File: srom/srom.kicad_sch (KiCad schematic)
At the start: 20 parts, among them J1 Conn_01x03_Female, Q1 PMBT2222A, U1 4075, U4 74LS245, U5 Pico-1 ROM

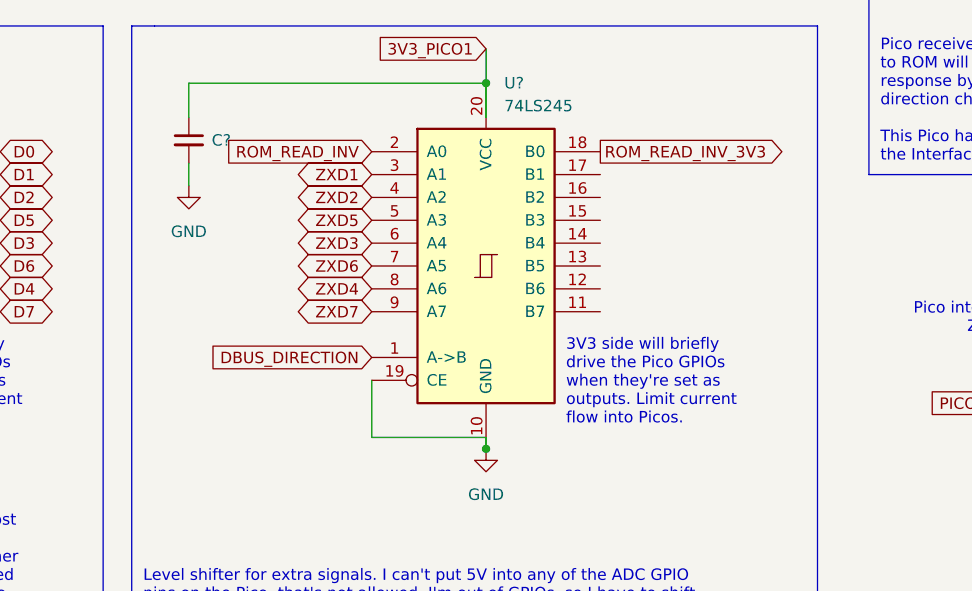
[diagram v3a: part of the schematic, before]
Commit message: update schematic to match current hardware
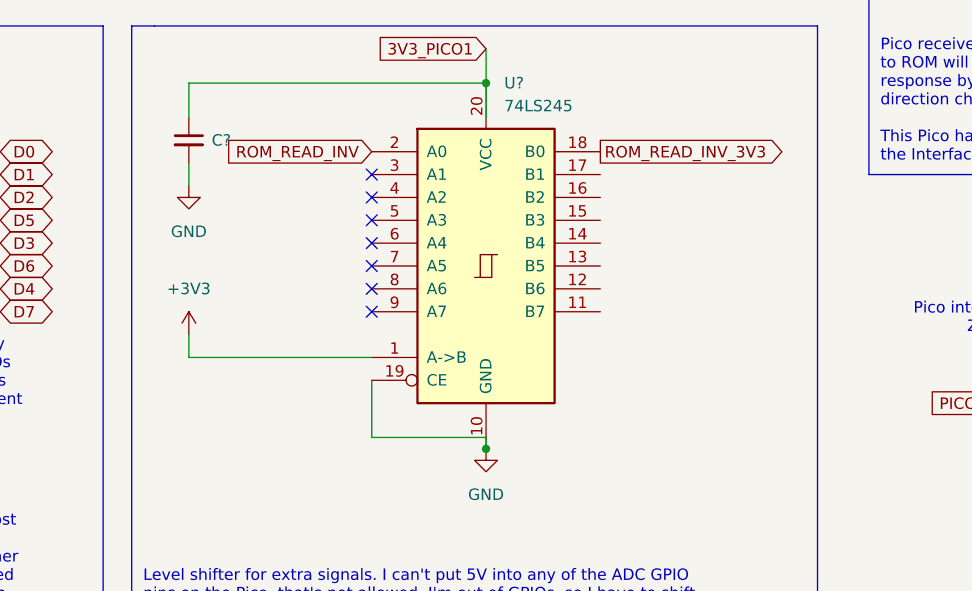
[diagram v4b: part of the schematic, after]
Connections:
- net DBUS_DIRECTION: no longer U?.1 (A->B)
- net ZXD1: no longer U?.3 (A1)
- net ZXD2: no longer U?.4 (A2)
- net ZXD3: no longer U?.6 (A4)
- net ZXD4: no longer U?.8 (A6)
- net ZXD5: no longer U?.5 (A3)
- net ZXD6: no longer U?.7 (A5)
- net ZXD7: no longer U?.9 (A7)
- new net +3V3: U?.1 (A->B)
- no-connect marks 27 -> 34
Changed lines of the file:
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@@
   (junction (at 132.715 156.21) (diameter 0) (color 0 0 0 0)
   )
+  (no_connect (at 120.015 125.73))
   (no_connect (at 54.61 62.23))
   (no_connect (at 54.61 29.21))
+  (no_connect (at 120.015 140.97))
   (no_connect (at 142.24 44.45))
   (no_connect (at 54.61 67.31))
+  (no_connect (at 120.015 128.27))
   (no_connect (at 26.67 29.21))
+  (no_connect (at 120.015 135.89))
   (no_connect (at 54.61 85.09))
+  (no_connect (at 120.015 133.35))
   (no_connect (at 26.67 57.15))
   (no_connect (at 54.61 59.69))
   (no_connect (at 54.61 57.15))
+  (no_connect (at 120.015 130.81))
   (no_connect (at 242.57 36.83))
   (no_connect (at 142.24 46.99))
@@
   (no_connect (at 26.67 52.07))
   (no_connect (at 142.24 41.91))
+  (no_connect (at 120.015 138.43))
   (no_connect (at 54.61 64.77))
   (no_connect (at 157.48 44.45))
@@
     (stroke (width 0) (type default) (color 0 0 0 0))
   )
+  (wire (pts (xy 99.695 143.51) (xy 99.695 146.05))
+    (stroke (width 0) (type default) (color 0 0 0 0))
+  )
   (polyline (pts (xy 280.67 125.73) (xy 175.26 125.73))
     (stroke (width 0) (type default) (color 0 0 0 0))
@@
   )
   (polyline (pts (xy 179.07 15.24) (xy 280.67 15.24))
+    (stroke (width 0) (type default) (color 0 0 0 0))
+  )
+  (wire (pts (xy 120.015 146.05) (xy 99.695 146.05))
     (stroke (width 0) (type default) (color 0 0 0 0))
   )
@@
     (effects (font (size 1.27 1.27)) (justify left bottom))
   )
-  (text "3V3 side will briefly\ndrive the Pico GPIOs\nwhen they're set as\noutputs. Limit current\nflow into Picos."
-    (at 141.605 153.67 0)
-    (effects (font (size 1.27 1.27)) (justify left bottom))
-  )
   (text "Level shifter for the data bus. Permanently enabled (unlike in the ROM\nemulator project). Direction is driven by the DBUS_DIRECTION signal. Most\ntimes that's high so the direction is ZX->Pico. The Pico therefore gets to\nsee any data the ZX writes pretty much immediately. During a read, either\n/MREQ or /IORQ, the direction is reversed by the signal which is generated\nvia a PIO program running on the IO Pico. That PIO responds to either the\n/MREQ or /IORQ, both of which the IO Pico can see."
     (at 15.24 175.26 0)
@@
     (effects (font (size 1.27 1.27)) (justify left bottom))
   )
-  (global_label "ZXD5" (shape bidirectional) (at 120.015 130.81 180) (fields_autoplaced)
-    (effects (font (size 1.27 1.27)) (justify right))
-    (property "Intersheet References" "${INTERSHEET_REFS}" (id 0) (at 112.7033 130.7306 0)
-      (effects (font (size 1.27 1.27)) (justify right) hide)
-    )
-  )
   (global_label "ZXD1" (shape bidirectional) (at 26.67 36.83 180) (fields_autoplaced)
     (effects (font (size 1.27 1.27)) (justify right))
@@
     )
   )
-  (global_label "DBUS_DIRECTION" (shape input) (at 120.015 146.05 180) (fields_autoplaced)
-    (effects (font (size 1.27 1.27)) (justify right))
-    (property "Intersheet References" "${INTERSHEET_REFS}" (id 0) (at 101.7571 145.9706 0)
-      (effects (font (size 1.27 1.27)) (justify right) hide)
-    )
-  )
   (global_label "D4" (shape input) (at 207.01 49.53 180) (fields_autoplaced)
     (effects (font (size 1.27 1.27)) (justify right))
@@
     )
   )
-  (global_label "ZXD7" (shape bidirectional) (at 120.015 140.97 180) (fields_autoplaced)
-    (effects (font (size 1.27 1.27)) (justify right))
-    (property "Intersheet References" "${INTERSHEET_REFS}" (id 0) (at 112.7033 140.8906 0)
-      (effects (font (size 1.27 1.27)) (justify right) hide)
-    )
-  )
   (global_label "ZXA1" (shape output) (at 54.61 44.45 0) (fields_autoplaced)
     (effects (font (size 1.27 1.27)) (justify left))
@@
     )
   )
-  (global_label "ZXD4" (shape bidirectional) (at 120.015 138.43 180) (fields_autoplaced)
-    (effects (font (size 1.27 1.27)) (justify right))
-    (property "Intersheet References" "${INTERSHEET_REFS}" (id 0) (at 112.7033 138.3506 0)
-      (effects (font (size 1.27 1.27)) (justify right) hide)
-    )
-  )
-  (global_label "ZXD3" (shape bidirectional) (at 120.015 133.35 180) (fields_autoplaced)
-    (effects (font (size 1.27 1.27)) (justify right))
-    (property "Intersheet References" "${INTERSHEET_REFS}" (id 0) (at 112.7033 133.2706 0)
-      (effects (font (size 1.27 1.27)) (justify right) hide)
-    )
-  )
   (global_label "ZXA14" (shape input) (at 87.63 44.45 180) (fields_autoplaced)
     (effects (font (size 1.27 1.27)) (justify right))
@@
     )
   )
-  (global_label "ZXD1" (shape bidirectional) (at 120.015 125.73 180) (fields_autoplaced)
-    (effects (font (size 1.27 1.27)) (justify right))
-    (property "Intersheet References" "${INTERSHEET_REFS}" (id 0) (at 112.7033 125.6506 0)
-      (effects (font (size 1.27 1.27)) (justify right) hide)
-    )
-  )
   (global_label "ZXA6" (shape input) (at 242.57 57.15 0) (fields_autoplaced)
     (effects (font (size 1.27 1.27)) (justify left))
@@
     )
   )
-  (global_label "ZXD6" (shape bidirectional) (at 120.015 135.89 180) (fields_autoplaced)
-    (effects (font (size 1.27 1.27)) (justify right))
-    (property "Intersheet References" "${INTERSHEET_REFS}" (id 0) (at 112.7033 135.8106 0)
-      (effects (font (size 1.27 1.27)) (justify right) hide)
-    )
-  )
   (global_label "ZXD5" (shape bidirectional) (at 40.64 130.81 180) (fields_autoplaced)
     (effects (font (size 1.27 1.27)) (justify right))
@@
     (effects (font (size 1.27 1.27)) (justify right))
     (property "Intersheet References" "${INTERSHEET_REFS}" (id 0) (at 198.6702 62.1506 0)
-      (effects (font (size 1.27 1.27)) (justify right) hide)
-    )
-  )
-  (global_label "ZXD2" (shape bidirectional) (at 120.015 128.27 180) (fields_autoplaced)
-    (effects (font (size 1.27 1.27)) (justify right))
-    (property "Intersheet References" "${INTERSHEET_REFS}" (id 0) (at 112.7033 128.1906 0)
       (effects (font (size 1.27 1.27)) (justify right) hide)
     )
@@
     )
     (property "Datasheet" "" (id 3) (at 53.34 156.21 0)
+      (effects (font (size 1.27 1.27)) hide)
+    )
+    (pin "1")
+  )
+  (symbol (lib_id "power:+3V3") (at 99.695 143.51 0) (unit 1)
+    (in_bom yes) (on_board yes) (fields_autoplaced)
+    (property "Reference" "#PWR?" (id 0) (at 99.695 147.32 0)
+      (effects (font (size 1.27 1.27)) hide)
+    )
+    (property "Value" "+3V3" (id 1) (at 99.695 138.43 0))
+    (property "Footprint" "" (id 2) (at 99.695 143.51 0)
+      (effects (font (size 1.27 1.27)) hide)
+    )
+    (property "Datasheet" "" (id 3) (at 99.695 143.51 0)
       (effects (font (size 1.27 1.27)) hide)
     )
@@
       (reference "#PWR?") (unit 1) (value "GND") (footprint "")
     )
+    (path "/7a0c9d83-3cea-4fe4-af9e-3086b3ce2ec9"
+      (reference "#PWR?") (unit 1) (value "+3V3") (footprint "")
+    )
     (path "/e8761be2-d56d-4ac2-8a7f-faeaa815f5d5"

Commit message: start updating schematic for next board
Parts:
- gave numbers to parts that had none: 2
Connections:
- net +3V3 is gone; now on net 3V3_PICO1: U101.1 (A->B)
- net D3: now also U5.5 (GPIO3); no longer U5.6 (GPIO4)
- net D4: now also U5.6 (GPIO4); no longer U5.9 (GPIO6)
- net D5: now also U5.7 (GPIO5); no longer U5.5 (GPIO3)
- net D6: now also U5.9 (GPIO6); no longer U5.7 (GPIO5)
- net ROM_READ_INV_3V3: now also U5.31 (GPIO26_ADC0); no longer U5.11 (GPIO8)
- net ZXA0: now also U5.11 (GPIO8); no longer U5.15 (GPIO11)
- net ZXA1: now also U5.12 (GPIO9); no longer U5.16 (GPIO12)
- net ZXA10: now also U5.24 (GPIO18); no longer U5.22 (GPIO17)
- net ZXA11: now also U5.25 (GPIO19); no longer U5.21 (GPIO16)
- net ZXA12: now also U5.26 (GPIO20); no longer U5.14 (GPIO10)
- net ZXA13: now also U5.27 (GPIO21); no longer U5.12 (GPIO9)
- net ZXA2: now also U5.14 (GPIO10); no longer U5.17 (GPIO13)
- net ZXA3: now also U5.15 (GPIO11); no longer U5.19 (GPIO14)
- net ZXA4: now also U5.16 (GPIO12); no longer U5.26 (GPIO20)
- net ZXA5: now also U5.17 (GPIO13); no longer U5.27 (GPIO21)
- net ZXA6: now also U5.19 (GPIO14); no longer U5.29 (GPIO22)
- net ZXA7: now also U5.20 (GPIO15); no longer U5.31 (GPIO26_ADC0)
- net ZXA8: now also U5.21 (GPIO16); no longer U5.25 (GPIO19)
- net ZXA9: now also U5.22 (GPIO17); no longer U5.24 (GPIO18)
- net ZXM1: now also U5.29 (GPIO22); no longer U5.20 (GPIO15)
- net IF1_PORT_ACTIVE: now reaches U5.32 (GPIO27_ADC1)
- no-connect marks 34 -> 40

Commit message: first draft of layout of board 2
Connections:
- net D3: now also R104.2; no longer R105.2
- net D4: now also R105.2; no longer R107.2
- net D5: now also R106.2; no longer R104.2
- net D6: now also R107.2; no longer R106.2
- net ZXD3: now also U4.5 (A3); no longer U4.6 (A4)
- net ZXD4: now also U4.6 (A4); no longer U4.8 (A6)
- net ZXD5: now also U4.7 (A5); no longer U4.5 (A3)
- net ZXD6: now also U4.8 (A6); no longer U4.7 (A5)
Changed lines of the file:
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@@
     )
   )
-  (global_label "D4" (shape bidirectional) (at 78.74 138.43 0) (fields_autoplaced)
+  (global_label "D6" (shape bidirectional) (at 78.74 138.43 0) (fields_autoplaced)
     (effects (font (size 1.27 1.27)) (justify left))
     (property "Intersheet References" "${INTERSHEET_REFS}" (id 0) (at 83.6326 138.3506 0)
@@
     )
   )
-  (global_label "ZXD6" (shape bidirectional) (at 40.64 135.89 180) (fields_autoplaced)
+  (global_label "ZXD5" (shape bidirectional) (at 40.64 135.89 180) (fields_autoplaced)
     (effects (font (size 1.27 1.27)) (justify right))
     (property "Intersheet References" "${INTERSHEET_REFS}" (id 0) (at 33.3283 135.8106 0)
@@
     )
   )
-  (global_label "ZXD4" (shape bidirectional) (at 40.64 138.43 180) (fields_autoplaced)
+  (global_label "ZXD6" (shape bidirectional) (at 40.64 138.43 180) (fields_autoplaced)
     (effects (font (size 1.27 1.27)) (justify right))
     (property "Intersheet References" "${INTERSHEET_REFS}" (id 0) (at 33.3283 138.3506 0)
@@
     )
   )
-  (global_label "D3" (shape bidirectional) (at 78.74 133.35 0) (fields_autoplaced)
+  (global_label "D4" (shape bidirectional) (at 78.74 133.35 0) (fields_autoplaced)
     (effects (font (size 1.27 1.27)) (justify left))
     (property "Intersheet References" "${INTERSHEET_REFS}" (id 0) (at 83.6326 133.2706 0)
@@
     )
   )
-  (global_label "ZXD5" (shape bidirectional) (at 40.64 130.81 180) (fields_autoplaced)
+  (global_label "ZXD3" (shape bidirectional) (at 40.64 130.81 180) (fields_autoplaced)
     (effects (font (size 1.27 1.27)) (justify right))
     (property "Intersheet References" "${INTERSHEET_REFS}" (id 0) (at 33.3283 130.7306 0)
@@
     )
   )
-  (global_label "D6" (shape bidirectional) (at 78.74 135.89 0) (fields_autoplaced)
+  (global_label "D5" (shape bidirectional) (at 78.74 135.89 0) (fields_autoplaced)
     (effects (font (size 1.27 1.27)) (justify left))
     (property "Intersheet References" "${INTERSHEET_REFS}" (id 0) (at 83.6326 135.8106 0)
@@
     )
   )
-  (global_label "D5" (shape bidirectional) (at 78.74 130.81 0) (fields_autoplaced)
+  (global_label "D3" (shape bidirectional) (at 78.74 130.81 0) (fields_autoplaced)
     (effects (font (size 1.27 1.27)) (justify left))
     (property "Intersheet References" "${INTERSHEET_REFS}" (id 0) (at 83.6326 130.7306 0)
@@
     )
   )
-  (global_label "ZXD3" (shape bidirectional) (at 40.64 133.35 180) (fields_autoplaced)
+  (global_label "ZXD4" (shape bidirectional) (at 40.64 133.35 180) (fields_autoplaced)
     (effects (font (size 1.27 1.27)) (justify right))
     (property "Intersheet References" "${INTERSHEET_REFS}" (id 0) (at 33.3283 133.2706 0)
@@
       (reference "#PWR0201") (unit 1) (value "GND") (footprint "")
     )
+    (path "/95a6eb69-d4c1-4a7e-a8e8-144430faf0e2/49643f1b-a3e7-406d-9651-75cb8bc3c20f"
+      (reference "#PWR0202") (unit 1) (value "GND") (footprint "")
+    )
     (path "/95a6eb69-d4c1-4a7e-a8e8-144430faf0e2/b4561307-559f-491e-95d1-1c57e89e9bd0"
       (reference "#PWR0203") (unit 1) (value "GND") (footprint "")
@@
       (reference "C101") (unit 1) (value "C_Small") (footprint "Capacitor_SMD:C_1206_3216Metric")
     )
+    (path "/95a6eb69-d4c1-4a7e-a8e8-144430faf0e2/bc372065-041b-4223-9621-9581521839ff"
+      (reference "C201") (unit 1) (value "C_Small") (footprint "Capacitor_SMD:C_1206_3216Metric")
+    )
     (path "/986f0686-4dd2-4d11-a20b-857347ffd112"

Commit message: more work on the layout of board 2
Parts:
- added J101: Conn_01x06_Female, Connector_PinHeader_2.54mm:PinHeader_1x06_P2.54mm_Vertical, symbol Connector:Conn_01x06_Female
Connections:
- net DBUS_DIRECTION: now also J101.6 (Pin_6)
- net IF1_PORT_ACTIVE: now also J101.3 (Pin_3)
- net PICO_RESET_Z80: now also J101.1 (Pin_1)
- net ROM_READ_INV_3V3: now also J101.4 (Pin_4)
- net ZXM1: now also J101.5 (Pin_5)
- net ZXRESET: now also J101.2 (Pin_2)
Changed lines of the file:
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@@
     (stroke (width 0) (type default) (color 0 0 0 0))
   )
-  (polyline (pts (xy 92.71 72.39) (xy 92.71 72.39))
+  (polyline (pts (xy 95.504 73.152) (xy 95.504 73.152))
     (stroke (width 0) (type default) (color 0 0 0 0))
   )
@@
   )
   (wire (pts (xy 99.695 124.46) (xy 99.695 127))
-    (stroke (width 0) (type default) (color 0 0 0 0))
-  )
-  (polyline (pts (xy 92.71 71.12) (xy 92.71 72.39))
     (stroke (width 0) (type default) (color 0 0 0 0))
   )
@@
     )
   )
+  (global_label "PICO_RESET_Z80" (shape output) (at 94.742 76.2 180) (fields_autoplaced)
+    (effects (font (size 1.27 1.27)) (justify right))
+    (property "Intersheet References" "${INTERSHEET_REFS}" (id 0) (at 76.5446 76.2794 0)
+      (effects (font (size 1.27 1.27)) (justify right) hide)
+    )
+  )
   (global_label "ZXA15" (shape output) (at 26.67 21.59 180) (fields_autoplaced)
     (effects (font (size 1.27 1.27)) (justify right))
@@
     )
   )
+  (global_label "ZXRESET" (shape output) (at 94.742 78.74 180) (fields_autoplaced)
+    (effects (font (size 1.27 1.27)) (justify right))
+    (property "Intersheet References" "${INTERSHEET_REFS}" (id 0) (at 84.1646 78.6606 0)
+      (effects (font (size 1.27 1.27)) (justify right) hide)
+    )
+  )
   (global_label "ZXD6" (shape bidirectional) (at 26.67 41.91 180) (fields_autoplaced)
     (effects (font (size 1.27 1.27)) (justify right))
@@
     )
   )
+  (global_label "ROM_READ_INV_3V3" (shape output) (at 94.742 83.82 180) (fields_autoplaced)
+    (effects (font (size 1.27 1.27)) (justify right))
+    (property "Intersheet References" "${INTERSHEET_REFS}" (id 0) (at 74.0651 83.8994 0)
+      (effects (font (size 1.27 1.27)) (justify right) hide)
+    )
+  )
   (global_label "ZXA11" (shape input) (at 242.57 67.31 0) (fields_autoplaced)
     (effects (font (size 1.27 1.27)) (justify left))
@@
     )
   )
+  (global_label "DBUS_DIRECTION" (shape output) (at 94.742 88.9 180) (fields_autoplaced)
+    (effects (font (size 1.27 1.27)) (justify right))
+    (property "Intersheet References" "${INTERSHEET_REFS}" (id 0) (at 76.4841 88.8206 0)
+      (effects (font (size 1.27 1.27)) (justify right) hide)
+    )
+  )
   (global_label "ROM_READ_INV" (shape input) (at 120.015 123.19 180) (fields_autoplaced)
     (effects (font (size 1.27 1.27)) (justify right))
@@
     )
   )
+  (global_label "ZXM1" (shape output) (at 94.742 86.36 180) (fields_autoplaced)
+    (effects (font (size 1.27 1.27)) (justify right))
+    (property "Intersheet References" "${INTERSHEET_REFS}" (id 0) (at 87.2489 86.4394 0)
+      (effects (font (size 1.27 1.27)) (justify right) hide)
+    )
+  )
   (global_label "ZXA12" (shape input) (at 242.57 64.77 0) (fields_autoplaced)
     (effects (font (size 1.27 1.27)) (justify left))
@@
     (effects (font (size 1.27 1.27)) (justify right))
     (property "Intersheet References" "${INTERSHEET_REFS}" (id 0) (at 181.1926 151.0506 0)
+      (effects (font (size 1.27 1.27)) (justify right) hide)
+    )
+  )
+  (global_label "IF1_PORT_ACTIVE" (shape output) (at 94.742 81.28 180) (fields_autoplaced)
+    (effects (font (size 1.27 1.27)) (justify right))
+    (property "Intersheet References" "${INTERSHEET_REFS}" (id 0) (at 76.4841 81.3594 0)
       (effects (font (size 1.27 1.27)) (justify right) hide)
     )
@@
     (pin "2")
   )
+  (symbol (lib_id "Connector:Conn_01x06_Female") (at 99.822 81.28 0) (unit 1)
+    (in_bom yes) (on_board yes) (fields_autoplaced)
+    (property "Reference" "J101" (id 0) (at 101.6 81.2799 0)
+      (effects (font (size 1.27 1.27)) (justify left))
+    )
+    (property "Value" "Conn_01x06_Female" (id 1) (at 101.6 83.8199 0)
+      (effects (font (size 1.27 1.27)) (justify left))
+    )
+    (property "Footprint" "Connector_PinHeader_2.54mm:PinHeader_1x06_P2.54mm_Vertical" (id 2) (at 99.822 81.28 0)
+      (effects (font (size 1.27 1.27)) hide)
+    )
+    (property "Datasheet" "~" (id 3) (at 99.822 81.28 0)
+      (effects (font (size 1.27 1.27)) hide)
+    )
+    (pin "1")
+    (pin "2")
+    (pin "3")
+    (pin "4")
+    (pin "5")
+    (pin "6")
+  )
   (symbol (lib_id "Device:R") (at 72.39 128.27 90) (unit 1)
     (in_bom yes) (on_board yes) (fields_autoplaced)
@@
       (reference "J1") (unit 1) (value "Conn_01x03_Female") (footprint "Connector_PinHeader_2.54mm:PinHeader_1x03_P2.54mm_Vertical")
     )
+    (path "/b001f89d-9f48-429a-b10f-bfc22b561bf3"
+      (reference "J101") (unit 1) (value "Conn_01x06_Female") (footprint "Connector_PinHeader_2.54mm:PinHeader_1x06_P2.54mm_Vertical")
+    )
     (path "/95a6eb69-d4c1-4a7e-a8e8-144430faf0e2/7fe63843-f758-4c7e-a4e3-75a239e41188"
       (reference "J201") (unit 1) (value "Conn_01x03_Female") (footprint "Connector_PinHeader_2.54mm:PinHeader_1x03_P2.54mm_Vertical")
     )
+    (path "/95a6eb69-d4c1-4a7e-a8e8-144430faf0e2/cd66f60d-1058-4213-bc50-c2c04efac531"
+      (reference "J202") (unit 1) (value "Conn_01x05_Female") (footprint "Connector_PinHeader_2.54mm:PinHeader_1x05_P2.54mm_Vertical")
+    )
     (path "/acda4c69-0a65-473b-ab4f-e765252d7da2/d6d0c58d-8e9e-45da-ac9c-b6edecaf4587"
